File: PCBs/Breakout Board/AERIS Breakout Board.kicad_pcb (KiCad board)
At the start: 2 copper layers, 57 x 22 mm, 10 parts, among them J1 Conn_01x05_Socket, J2 Conn_01x02_Socket, J3 Conn_01x05_Socket, Q1 2N3904, U1 ESP32C3

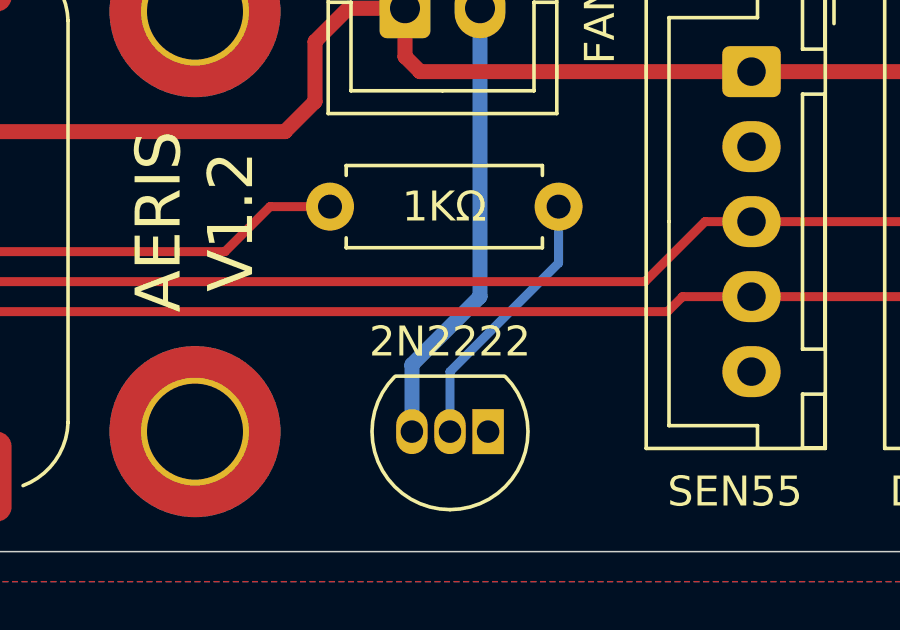
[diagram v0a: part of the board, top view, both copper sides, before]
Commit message: Added PCB CAD
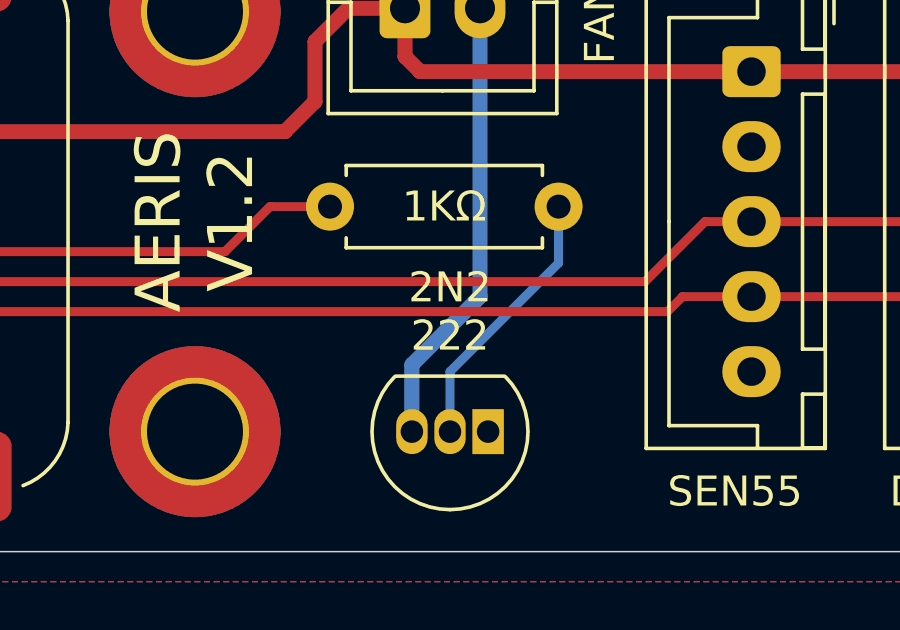
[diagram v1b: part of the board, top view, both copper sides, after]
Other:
- board text added: "2N2 222"
- board text removed: "2N2222"
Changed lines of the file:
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@@
 		)
 		(embedded_fonts no)
-		(model "${KIPRJMOD}/STEP/XIAO_ESP32C3.STEP"
+		(model "/Users/alex/Documents/GitHub/AERIS/CAD/Reference/Seeed Studio XIAO-ESP32-C3.step"
 			(offset
 				(xyz 0 0 0)
@@
 			)
 			(rotate
-				(xyz -90 -0 -0)
+				(xyz -0 -0 -180)
 			)
 		)
@@
 		(layer "Edge.Cuts")
 	)
-	(gr_text "2N2222"
-		(at 155.5 104 0)
+	(gr_text "2N2\n222"
+		(at 155.5 103 0)
 		(layer "F.SilkS")
 		(effects

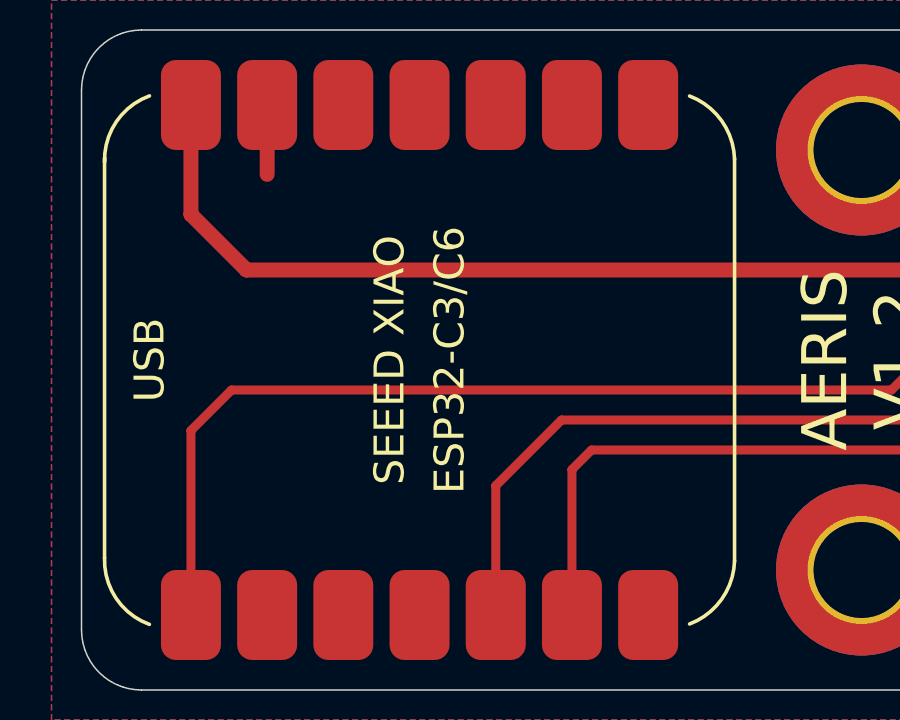
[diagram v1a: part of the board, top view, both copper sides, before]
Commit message: Update PCBs
Swap to just ESP32C6
Make footprint libraries project and not global
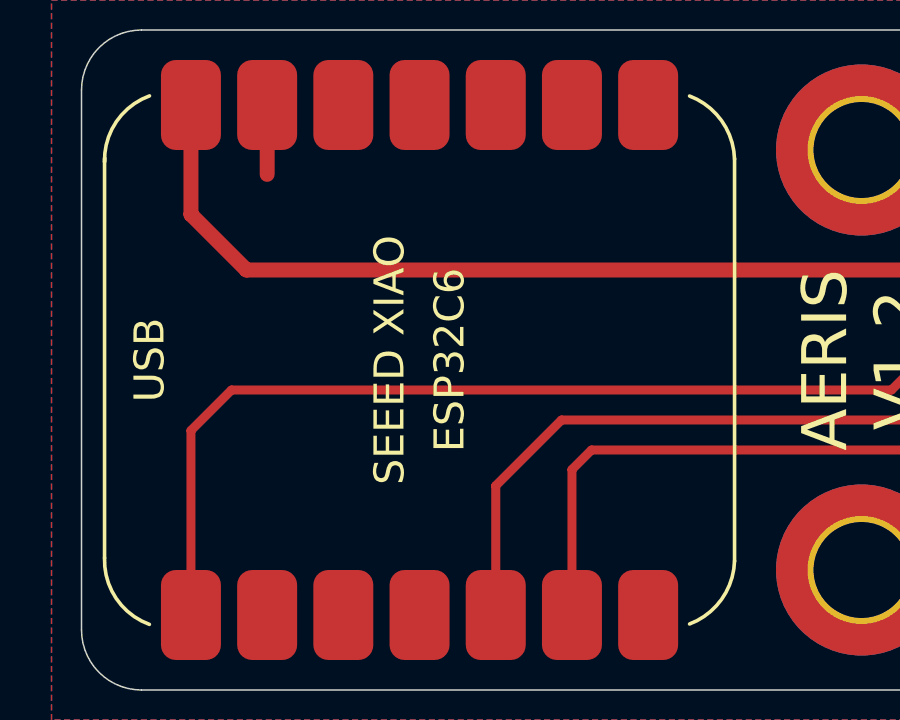
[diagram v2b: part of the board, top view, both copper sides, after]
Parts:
- J1, J3: footprint Custom Footprints:JST_XH_B5B-XH-A_1x05_P2.50mm_Vertical -> Library:JST_XH_B5B-XH-A_1x05_P2.50mm_Vertical
- J2: footprint Custom Footprints:JST_XH_B2B-XH-A_1x02_P2.50mm_Vertical -> Library:JST_XH_B2B-XH-A_1x02_P2.50mm_Vertical
- Q1: footprint Custom Footprints:TO-92_Inline -> Library:TO-92_Inline
- R1: footprint Custom Footprints:R_Axial_DIN0207_L6.3mm_D2.5mm_P7.62mm_Horizontal -> Library:R_Axial_DIN0207_L6.3mm_D2.5mm_P7.62mm_Horizontal
- REF** (x2): footprint MountingHole:MountingHole_3.2mm_M3_ISO7380_Pad_TopBottom -> Library:MountingHole_3.2mm_M3_ISO7380_Pad_TopBottom
- REF**: footprint Symbol:KiCad-Logo2_5mm_SilkScreen -> Library:KiCad-Logo2_5mm_SilkScreen
- REF**: footprint Symbol:Symbol_GNU-Logo_SilkscreenTop -> Library:Symbol_GNU-Logo_SilkscreenTop
- U1: footprint Custom Footprints:XIAO_ESP32 -> Library:XIAO_ESP32
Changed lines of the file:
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@@
 	(net 15 "unconnected-(U1-D9-Pad10)")
 	(net 16 "unconnected-(U1-VCC_3V3-Pad12)")
-	(footprint "Custom Footprints:JST_XH_B5B-XH-A_1x05_P2.50mm_Vertical"
+	(footprint "Library:JST_XH_B5B-XH-A_1x05_P2.50mm_Vertical"
 		(layer "F.Cu")
 		(at 173.5 95 -90)
@@
 		)
 	)
-	(footprint "Custom Footprints:TO-92_Inline"
+	(footprint "Library:TO-92_Inline"
 		(layer "F.Cu")
 		(at 156.77 107 180)
@@
 		)
 	)
-	(footprint "MountingHole:MountingHole_3.2mm_M3_ISO7380_Pad_TopBottom"
+	(footprint "Library:MountingHole_3.2mm_M3_ISO7380_Pad_TopBottom"
 		(layer "F.Cu")
 		(at 147 93)
@@
 		(embedded_fonts no)
 	)
-	(footprint "Custom Footprints:XIAO_ESP32"
+	(footprint "Library:XIAO_ESP32"
 		(layer "F.Cu")
 		(at 132.268 100 90)
@@
 			)
 		)
-		(fp_text user "ESP32-C3/C6"
+		(fp_text user "ESP32C6"
 			(at 0 1 90)
 			(unlocked yes)
@@
 		)
 		(embedded_fonts no)
-		(model "/Users/alex/Documents/GitHub/AERIS/CAD/Reference/Seeed Studio XIAO-ESP32-C3.step"
+		(model "/Users/alex/Documents/GitHub/AERIS/CAD/Reference/Seeed Studio XIAO ESP32-C6.step"
 			(offset
 				(xyz 0 0 0)
@@
 		)
 	)
-	(footprint "Custom Footprints:JST_XH_B5B-XH-A_1x05_P2.50mm_Vertical"
+	(footprint "Library:JST_XH_B5B-XH-A_1x05_P2.50mm_Vertical"
 		(layer "F.Cu")
 		(at 165.55 95 -90)
@@
 		)
 	)
-	(footprint "Custom Footprints:JST_XH_B2B-XH-A_1x02_P2.50mm_Vertical"
+	(footprint "Library:JST_XH_B2B-XH-A_1x02_P2.50mm_Vertical"
 		(layer "F.Cu")
 		(at 154 92.888)
@@
 		)
 	)
-	(footprint "MountingHole:MountingHole_3.2mm_M3_ISO7380_Pad_TopBottom"
+	(footprint "Library:MountingHole_3.2mm_M3_ISO7380_Pad_TopBottom"
 		(layer "F.Cu")
 		(at 147 107)
@@
 		(embedded_fonts no)
 	)
-	(footprint "Custom Footprints:R_Axial_DIN0207_L6.3mm_D2.5mm_P7.62mm_Horizontal"
+	(footprint "Library:R_Axial_DIN0207_L6.3mm_D2.5mm_P7.62mm_Horizontal"
 		(layer "F.Cu")
 		(at 151.5 99.5)
@@
 		)
 	)
-	(footprint "Symbol:KiCad-Logo2_5mm_SilkScreen"
+	(footprint "Library:KiCad-Logo2_5mm_SilkScreen"
 		(layer "B.Cu")
 		(at 125.92393 100 -90)
@@
 		(embedded_fonts no)
 	)
-	(footprint "Symbol:Symbol_GNU-Logo_SilkscreenTop"
+	(footprint "Library:Symbol_GNU-Logo_SilkscreenTop"
 		(layer "B.Cu")
 		(at 134.92393 100 -90)

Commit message: Production Check
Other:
- board text added: "2N2222"
- board text removed: "2N2 222"
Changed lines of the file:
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@@
 		(layer "Edge.Cuts")
 	)
-	(gr_text "2N2\n222"
-		(at 155.5 103 0)
+	(gr_text "2N2222"
+		(at 155.5 103.5 0)
 		(layer "F.SilkS")
 		(effects
